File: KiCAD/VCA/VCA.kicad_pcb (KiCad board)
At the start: 2 copper layers, 40 x 53 mm, 15 parts, among them J1 VIN, J2 VC, J3 VOUT, J4 Conn_01x03_Pin, Q1 J172, Q2 J172, U1 LT1006

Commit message: VCA PCB
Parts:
- added Ref**: Val**, HackSynth:PancakeLegend Logo - 10mm, B.Cu at (137.5, 132.0)
- added Ref**: Val**, HackSynth:CCHS Logo - 10mm, B.Cu at (137.5, 120.5)
- moved J4 88.1 mm to (135.5, 143.6)
- moved R5 79.3 mm to (130.0, 132.9), turned to -90 degrees
- moved RV2 78.8 mm to (125.0, 123.2)
- moved J2 76.2 mm to (122.5, 136.2)
- moved RV1 75.2 mm to (125.0, 77.4)
- moved R4 75.1 mm to (141.2, 101.9)
- moved R3 74.9 mm to (137.5, 101.9)
- moved Q1 71.4 mm to (125.2, 110.0)
- moved C1 71.0 mm to (132.5, 89.0)
- moved U1 71.0 mm to (126.2, 94.2)
- moved Q2 70.6 mm to (132.2, 110.0)
- moved J3 68.5 mm to (137.5, 65.0)
- moved R2 67.3 mm to (122.5, 94.2)
- moved R1 67.1 mm to (118.8, 94.2)
- moved J1 58.1 mm to (122.5, 65.0)
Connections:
- J1 pad S: unconnected-(J1-PadS) -> GND
- J2 pad S: unconnected-(J2-PadS) -> GND
- J3 pad S: unconnected-(J3-PadS) -> GND
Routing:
- net Net-(J3-PadT): track 0.00 -> 43.9 mm
- net Net-(J1-PadT): track 0.00 -> 37.8 mm
- net Net-(Q1-D): track 0.00 -> 35.5 mm
- net Net-(Q2-D): track 0.00 -> 33.1 mm
- net Net-(R5-Pad2): track 0.00 -> 19.4 mm
- net Net-(R2-Pad1): track 0.00 -> 19.3 mm
- net Net-(J2-PadT): track 0.00 -> 12.9 mm
- net Net-(Q1-G): track 0.00 -> 12.3 mm
- added copper zone on B.Cu, net GND
- added copper zone on F.Cu, net GND
- added copper zone on In1.Cu, net VDD
- added copper zone on In2.Cu, net VSS
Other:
- board size 40 x 53 mm -> 30 x 100 mm
- copper layers 2 -> 4
- board text added: "CV"
- board text added: "IN"
- board text added: "OUT"
- board text added: "VCA v1-0 - PancakeLegend 2025"

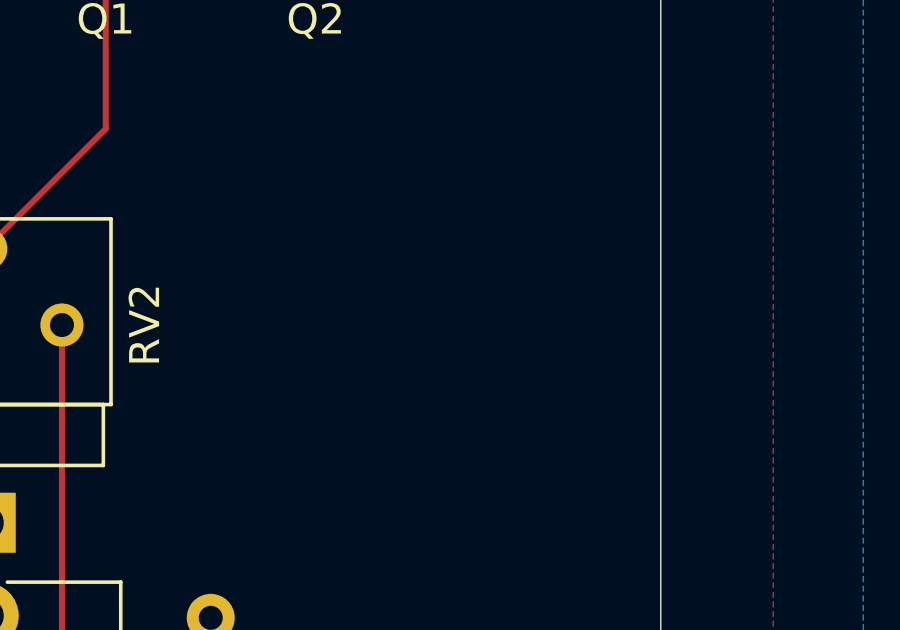
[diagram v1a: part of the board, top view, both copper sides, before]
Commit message: 3.5mm Jack
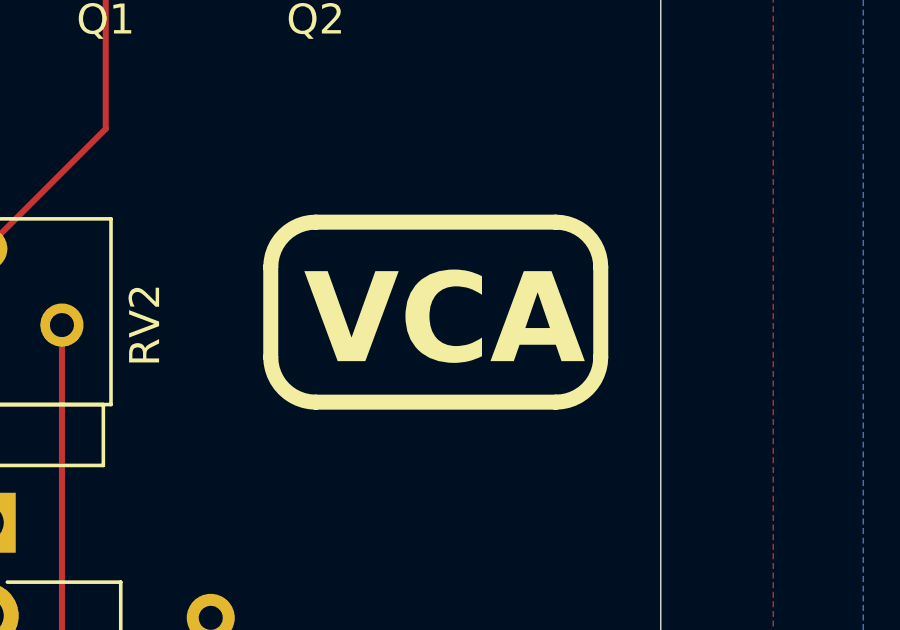
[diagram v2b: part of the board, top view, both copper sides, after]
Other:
- board text added: "VCA"
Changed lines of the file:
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@@
 		)
 		(embedded_fonts no)
-		(model "C:/Users/ocd/OneDrive/Drafting/CCHS/HackSynth/KiCAD/HackSynth.pretty/3.5mm_Jack_Vert.stp"
+		(model "C:/Users/ocd/OneDrive/Drafting/CCHS/HackSynth/KiCAD/HackSynth.pretty/3.5mm_Jack_Vert.step"
 			(offset
-				(xyz 0 0 14.5)
+				(xyz 0 0 0)
 			)
 			(scale
@@
 			)
 			(rotate
-				(xyz -0 -90 -0)
+				(xyz -0 -0 -0)
 			)
 		)
@@
 		)
 		(embedded_fonts no)
-		(model "C:/Users/ocd/OneDrive/Drafting/CCHS/HackSynth/KiCAD/HackSynth.pretty/3.5mm_Jack_Vert.stp"
+		(model "C:/Users/ocd/OneDrive/Drafting/CCHS/HackSynth/KiCAD/HackSynth.pretty/3.5mm_Jack_Vert.step"
 			(offset
-				(xyz 0 0 14.5)
+				(xyz 0 0 0)
 			)
 			(scale
@@
 			)
 			(rotate
-				(xyz -0 -90 -0)
+				(xyz -0 -0 -0)
 			)
 		)
@@
 		)
 		(embedded_fonts no)
-		(model "C:/Users/ocd/OneDrive/Drafting/CCHS/HackSynth/KiCAD/HackSynth.pretty/3.5mm_Jack_Vert.stp"
+		(model "C:/Users/ocd/OneDrive/Drafting/CCHS/HackSynth/KiCAD/HackSynth.pretty/3.5mm_Jack_Vert.step"
 			(offset
-				(xyz 0 0 14.5)
+				(xyz 0 0 0)
 			)
 			(scale
@@
 			)
 			(rotate
-				(xyz -0 -90 -0)
+				(xyz -0 -0 -0)
 			)
 		)
@@
 	)
 	(gr_arc
+		(start 141.5 119.75)
+		(mid 142.56066 120.18934)
+		(end 143 121.25)
+		(stroke
+			(width 0.5)
+			(type solid)
+		)
+		(layer "F.SilkS")
+	)
+	(gr_arc
+		(start 143.000001 124.250001)
+		(mid 142.560661 125.310661)
+		(end 141.500001 125.750001)
+		(stroke
+			(width 0.5)
+			(type solid)
+		)
+		(layer "F.SilkS")
+	)
+	(gr_line
+		(start 143 121.25)
+		(end 143 124.25)
+		(stroke
+			(width 0.5)
+			(type solid)
+		)
+		(layer "F.SilkS")
+	)
+	(gr_line
+		(start 133.5 119.749999)
+		(end 141.5 119.75)
+		(stroke
+			(width 0.5)
+			(type solid)
+		)
+		(layer "F.SilkS")
+	)
+	(gr_arc
+		(start 131.999999 121.249999)
+		(mid 132.439339 120.189339)
+		(end 133.499999 119.749999)
+		(stroke
+			(width 0.5)
+			(type solid)
+		)
+		(layer "F.SilkS")
+	)
+	(gr_arc
+		(start 133.499999 125.750001)
+		(mid 132.439339 125.310661)
+		(end 131.999999 124.250001)
+		(stroke
+			(width 0.5)
+			(type solid)
+		)
+		(layer "F.SilkS")
+	)
+	(gr_line
+		(start 131.999999 121.249999)
+		(end 131.999999 124.249999)
+		(stroke
+			(width 0.5)
+			(type solid)
+		)
+		(layer "F.SilkS")
+	)
+	(gr_line
+		(start 133.499999 125.75)
+		(end 141.500001 125.750001)
+		(stroke
+			(width 0.5)
+			(type solid)
+		)
+		(layer "F.SilkS")
+	)
+	(gr_arc
 		(start 144.999999 147)
 		(mid 144.121319 149.12132)
@@
 		)
 	)
+	(gr_text "VCA"
+		(at 133.1 124.75 0)
+		(layer "F.SilkS")
+		(effects
+			(font
+				(size 3 3)
+				(thickness 0.5)
+				(bold yes)
+			)
+			(justify left bottom)
+		)
+	)
